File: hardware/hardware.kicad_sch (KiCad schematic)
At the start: 0 parts

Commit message: added microcontroller into kicad
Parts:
- added U1: STM32F103C8Tx, Package_QFP:LQFP-48_7x7mm_P0.5mm, symbol MCU_ST_STM32F1:STM32F103C8Tx
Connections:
- new net: U1.23 (VSS), U1.35 (VSS), U1.47 (VSS)
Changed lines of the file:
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@@
 (kicad_sch
-	(version 20250114)
+	(version 20260306)
 	(generator "eeschema")
-	(generator_version "9.0")
+	(generator_version "10.0")
 	(paper "A4")
+	(symbol
+		(lib_id "MCU_ST_STM32F1:STM32F103C8Tx")
+		(at 175.26 76.2 0)
+		(unit 1)
+		(body_style 1)
+		(exclude_from_sim no)
+		(in_bom yes)
+		(on_board yes)
+		(in_pos_files yes)
+		(dnp no)
+		(fields_autoplaced yes)
+		(property "Reference" "U1"
+			(at 179.9433 116.84 0)
+			(show_name no)
+			(do_not_autoplace no)
+			(effects
+				(font
+					(size 1.27 1.27)
+				)
+				(justify left)
+			)
+		)
+		(property "Value" "STM32F103C8Tx"
+			(at 179.9433 119.38 0)
+			(show_name no)
+			(do_not_autoplace no)
+			(effects
+				(font
+					(size 1.27 1.27)
+				)
+				(justify left)
+			)
+		)
+		(property "Footprint" "Package_QFP:LQFP-48_7x7mm_P0.5mm"
+			(at 160.02 114.3 0)
+			(hide yes)
+			(show_name no)
+			(do_not_autoplace no)
+			(effects
+				(font
+					(size 1.27 1.27)
+				)
+				(justify right)
+			)
+		)
+		(property "Datasheet" "https://www.st.com/resource/en/datasheet/stm32f103c8.pdf"
+			(at 175.26 76.2 0)
+			(hide yes)
+			(show_name no)
+			(do_not_autoplace no)
+			(effects
+				(font
+					(size 1.27 1.27)
+				)
+			)
+		)
+		(property "Description" "STMicroelectronics Arm Cortex-M3 MCU, 64KB flash, 20KB RAM, 72 MHz, 2.0-3.6V, 37 GPIO, LQFP48"
+			(at 175.26 76.2 0)
+			(hide yes)
+			(show_name no)
+			(do_not_autoplace no)
+			(effects
+				(font
+					(size 1.27 1.27)
+				)
+			)
+		)
+		(pin "18"
+		)
+		(pin "9"
+		)
+		(pin "6"
+		)
+		(pin "22"
+		)
+		(pin "27"
+		)
+		(pin "1"
+		)
+		(pin "8"
+		)
+		(pin "11"
+		)
+		(pin "2"
+		)
+		(pin "16"
+		)
+		(pin "19"
+		)
+		(pin "20"
+		)
+		(pin "7"
+		)
+		(pin "13"
+		)
+		(pin "3"
+		)
+		(pin "14"
+		)
+		(pin "12"
+		)
+		(pin "15"
+		)
+		(pin "21"
+		)
+		(pin "4"
+		)
+		(pin "17"
+		)
+		(pin "10"
+		)
+		(pin "23"
+		)
+		(pin "5"
+		)
+		(pin "24"
+		)
+		(pin "25"
+		)
+		(pin "26"
+		)
+		(pin "39"
+		)
+		(pin "44"
+		)
+		(pin "37"
+		)
+		(pin "38"
+		)
+		(pin "34"
+		)
+		(pin "47"
+		)
+		(pin "41"
+		)
+		(pin "30"
+		)
+		(pin "40"
+		)
+		(pin "45"
+		)
+		(pin "32"
+		)
+		(pin "36"
+		)
+		(pin "42"
+		)
+		(pin "33"
+		)
+		(pin "28"
+		)
+		(pin "29"
+		)
+		(pin "35"
+		)
+		(pin "31"
+		)
+		(pin "43"
+		)
+		(pin "46"
+		)
+		(pin "48"
+		)
+		(instances
+			(project "hardware"
+				(path "/966ea169-4ce0-4fe7-960e-f81f04947f18"
+					(reference "U1")
+					(unit 1)
+				)
+			)
+		)
+	)
 	(sheet_instances
 		(path "/"

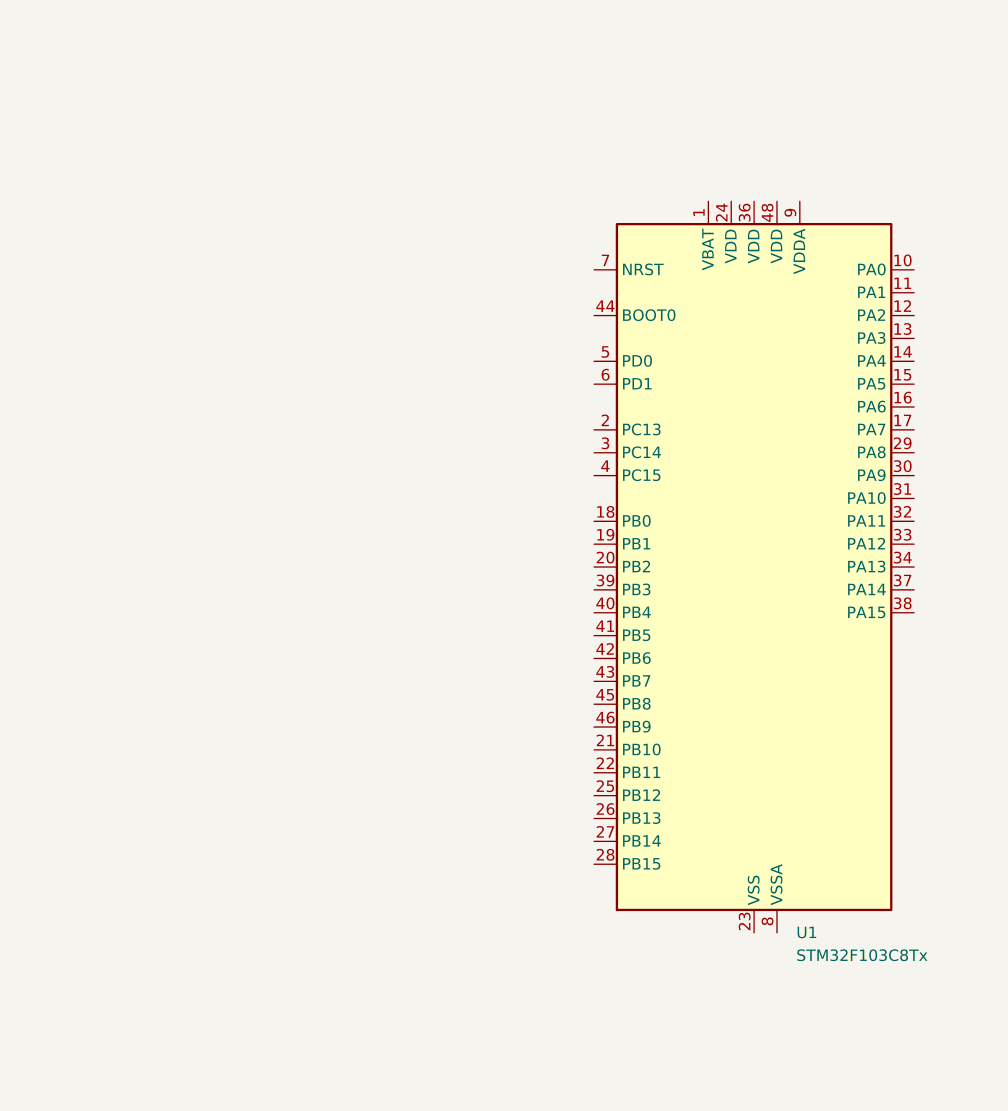
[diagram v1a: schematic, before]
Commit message: Update hardware schematic; ignore KiCad lock and history files
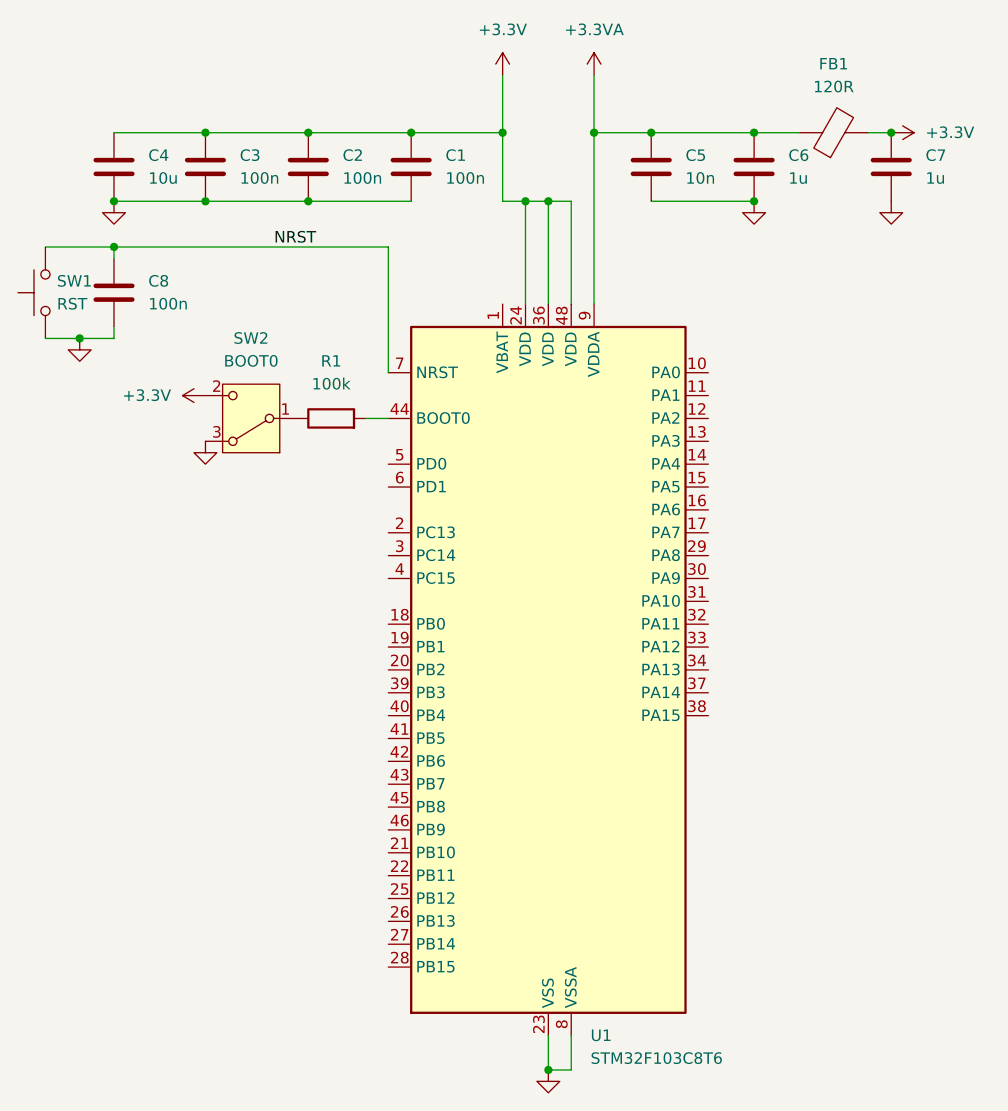
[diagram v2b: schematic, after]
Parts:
- added C1, C2, C3, C8: 100n, symbol Device:C
- added C4: 10u, symbol Device:C
- added C5: 10n, symbol Device:C
- added C6, C7: 1u, symbol Device:C
- added FB1: 120R, symbol Device:FerriteBead
- added R1: 100k, symbol Device:R
- added SW1: RST, symbol Switch:SW_Push
- added SW2: BOOT0, symbol Switch:SW_SPDT_312
- U1: value STM32F103C8Tx -> STM32F103C8T6
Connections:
- net at U1.23 (VSS), U1.35 (VSS), U1.47 (VSS): now also U1.8 (VSSA)
- net +3.3V: now reaches U1.24 (VDD)
- net +3.3V: now also U1.36 (VDD), U1.48 (VDD), C1.1, C2.1, C3.1, C4.1, C7.1, FB1.2, SW2.2 (C)
- net at U1.44 (BOOT0): now also R1.2
- net NRST: now reaches U1.7 (NRST)
- net NRST: now also C8.1, SW1.2
- net +3.3VA: now reaches U1.9 (VDDA)
- net +3.3VA: now also C5.1, C6.1, FB1.1
- new net: C5.2, C6.2
- new net: C1.2, C2.2, C3.2, C4.2
- new net: R1.1, SW2.1 (B)
- new net: C8.2, SW1.1

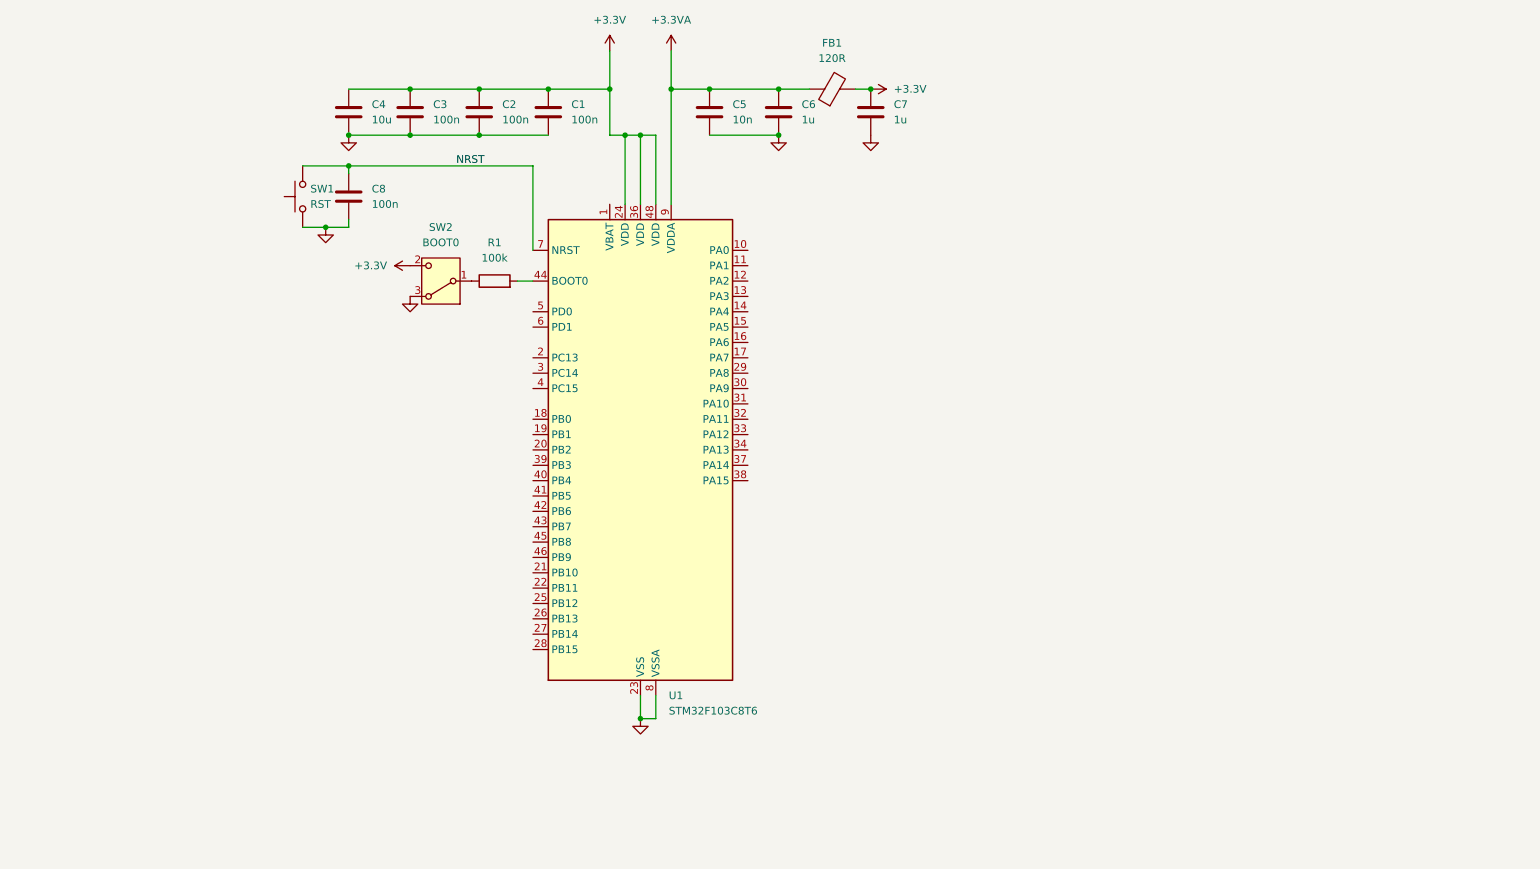
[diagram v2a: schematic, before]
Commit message: added usb and serial debug interface in schematic
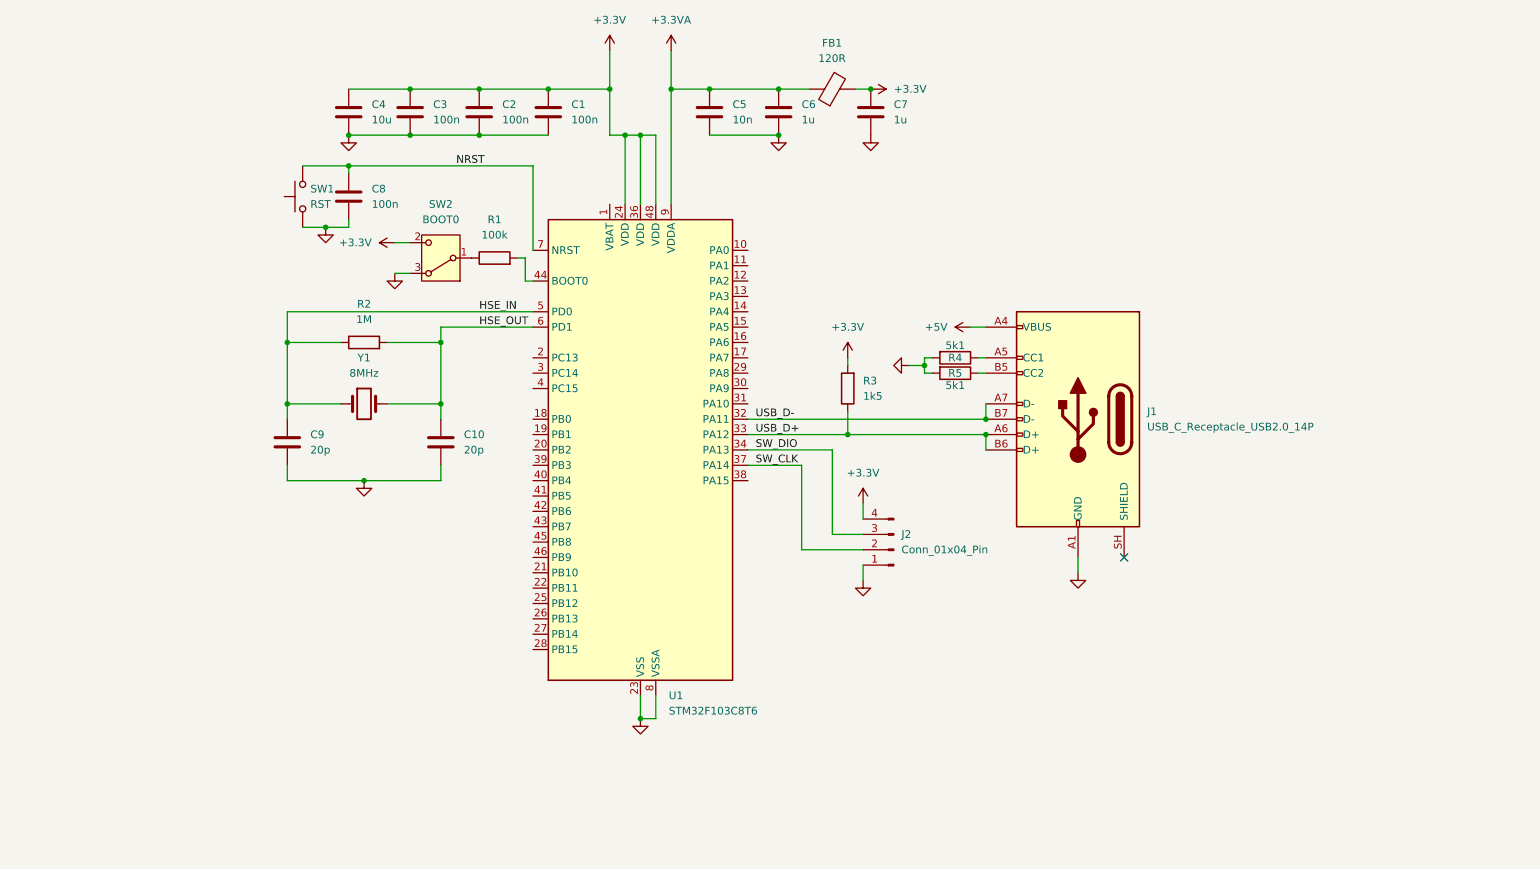
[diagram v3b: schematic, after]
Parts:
- added C10, C9: 20p, symbol Device:C
- added J1: USB_C_Receptacle_USB2.0_14P, symbol Connector:USB_C_Receptacle_USB2.0_14P
- added J2: Conn_01x04_Pin, symbol Connector:Conn_01x04_Pin
- added R2: 1M, symbol Device:R
- added R3: 1k5, symbol Device:R
- added R4, R5: 5k1, symbol Device:R
- added Y1: 8MHz, symbol Device:Crystal
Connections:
- net +3.3V: now also J2.4 (Pin_4), R3.2
- net USB_D-: now reaches U1.32 (PA11)
- net USB_D-: now also J1.A7 (D-), J1.B7 (D-)
- net USB_D+: now reaches U1.33 (PA12)
- net USB_D+: now also J1.A6 (D+), J1.B6 (D+), R3.1
- net SW_DIO: now reaches U1.34 (PA13)
- net SW_DIO: now also J2.3 (Pin_3)
- net SW_CLK: now reaches U1.37 (PA14)
- net SW_CLK: now also J2.2 (Pin_2)
- net HSE_IN: now reaches U1.5 (PD0)
- net HSE_IN: now also C9.1, R2.1, Y1.1
- net HSE_OUT: now reaches U1.6 (PD1)
- net HSE_OUT: now also C10.1, R2.2, Y1.2
- new net: C10.2, C9.2
- new net: J1.A1 (GND), J1.A12 (GND), J1.B1 (GND), J1.B12 (GND)
- new net: J1.A5 (CC1), R4.1
- new net: J1.B5 (CC2), R5.1
- new net: R4.2, R5.2
- new net +5V: J1.A4 (VBUS), J1.A9 (VBUS), J1.B4 (VBUS), J1.B9 (VBUS)
- no-connect marks 0 -> 1
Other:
- moved on the sheet: R1, SW2

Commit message: configured more spi/io pins in cubemx
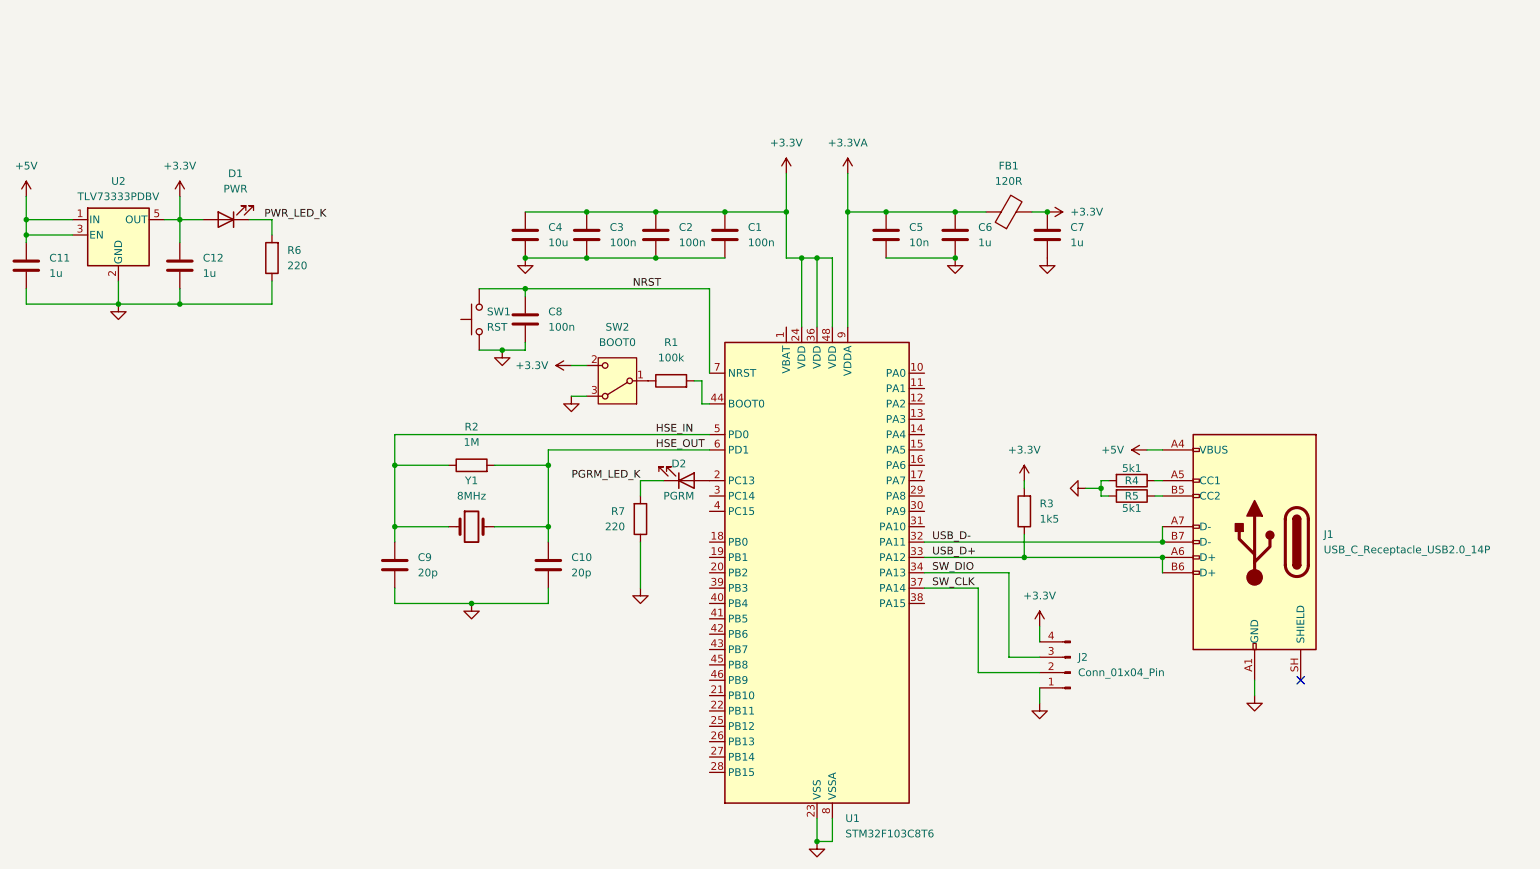
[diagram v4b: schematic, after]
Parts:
- added C11, C12: 1u, symbol Device:C
- added D1: PWR, symbol Device:LED
- added D2: PGRM, symbol Device:LED
- added R6, R7: 220, symbol Device:R
- added U2: TLV73333PDBV, Package_TO_SOT_SMD:SOT-23-5, symbol Regulator_Linear:TLV73333PDBV
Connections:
- net +3.3V: now also C12.1, D1.2 (A), U2.5 (OUT)
- net +5V: now also C11.1, U2.1 (IN), U2.3 (EN)
- net at U1.2 (PC13): now also D2.2 (A)
- new net: C11.2, C12.2, R6.1, U2.2 (GND)
- new net PGRM_LED_K: D2.1 (K), R7.2
- new net PWR_LED_K: D1.1 (K), R6.2
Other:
- moved on the sheet: C1, C10, C2, C3, C4, C5, C6, C7, C8, C9, FB1, J1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
